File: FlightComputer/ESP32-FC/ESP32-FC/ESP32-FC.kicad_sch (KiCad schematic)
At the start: 0 parts

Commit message: Added USB Connection
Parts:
- added C1: C, symbol Device:C
- added J1: USB_C_Receptacle_USB2.0_16P, symbol Connector:USB_C_Receptacle_USB2.0_16P
- added R1: R, symbol Device:R
- added R2, R3: 5K1, symbol Device:R
- added R4, R5: 27, symbol Device:R
- added U1: ESP32-S3-WROOM-1, RF_Module:ESP32-S3-WROOM-1, symbol RF_Module:ESP32-S3-WROOM-1
- added U2: AP2112K-3.3, Package_TO_SOT_SMD:SOT-23-5, symbol Regulator_Linear:AP2112K-3.3
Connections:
- new net: J1.A5 (CC1), R2.1
- new net: J1.B5 (CC2), R3.1
- new net +5V: J1.A4 (VBUS), J1.A9 (VBUS), J1.B4 (VBUS), J1.B9 (VBUS)
- new net GND: J1.A1 (GND), J1.A12 (GND), J1.B1 (GND), J1.B12 (GND), J1.S1 (SHIELD), R2.2, R3.2, U1.1 (GND), U1.40 (GND), U1.41 (GND)
- new net USB_D+: J1.A6 (D+), J1.B6 (D+), R5.1, R5.2, U1.14 (USB_D+)
- new net USB_D-: J1.A7 (D-), J1.B7 (D-), R4.1, R4.2, U1.13 (USB_D-)
- no-connect marks 0 -> 2

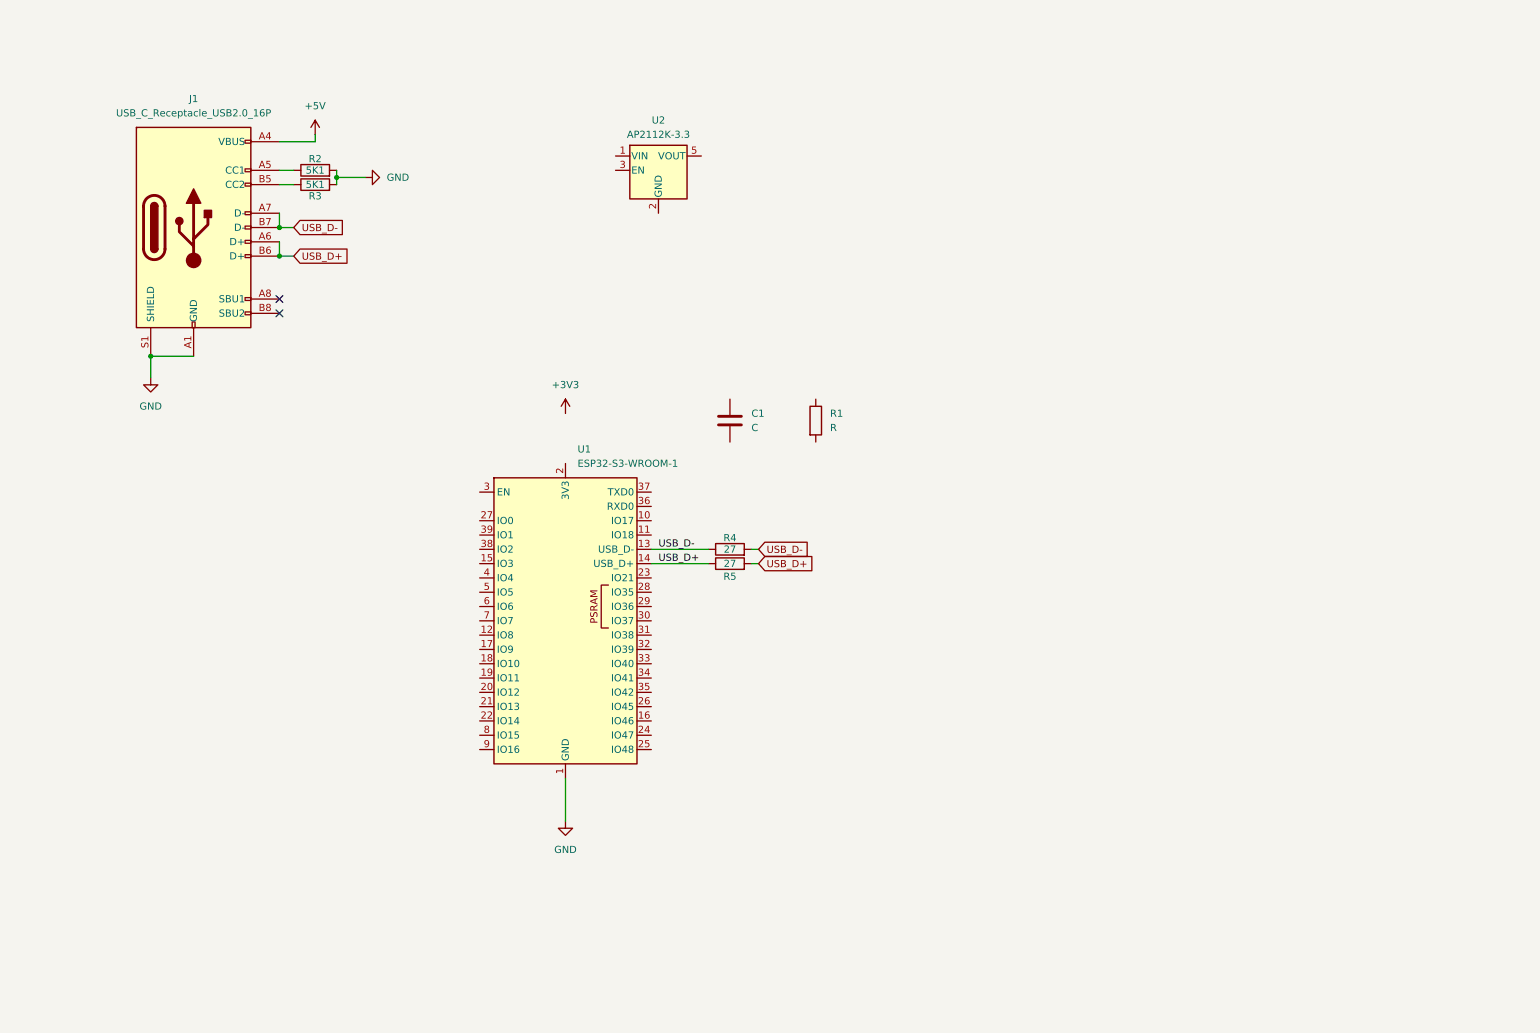
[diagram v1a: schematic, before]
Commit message: Added MPU
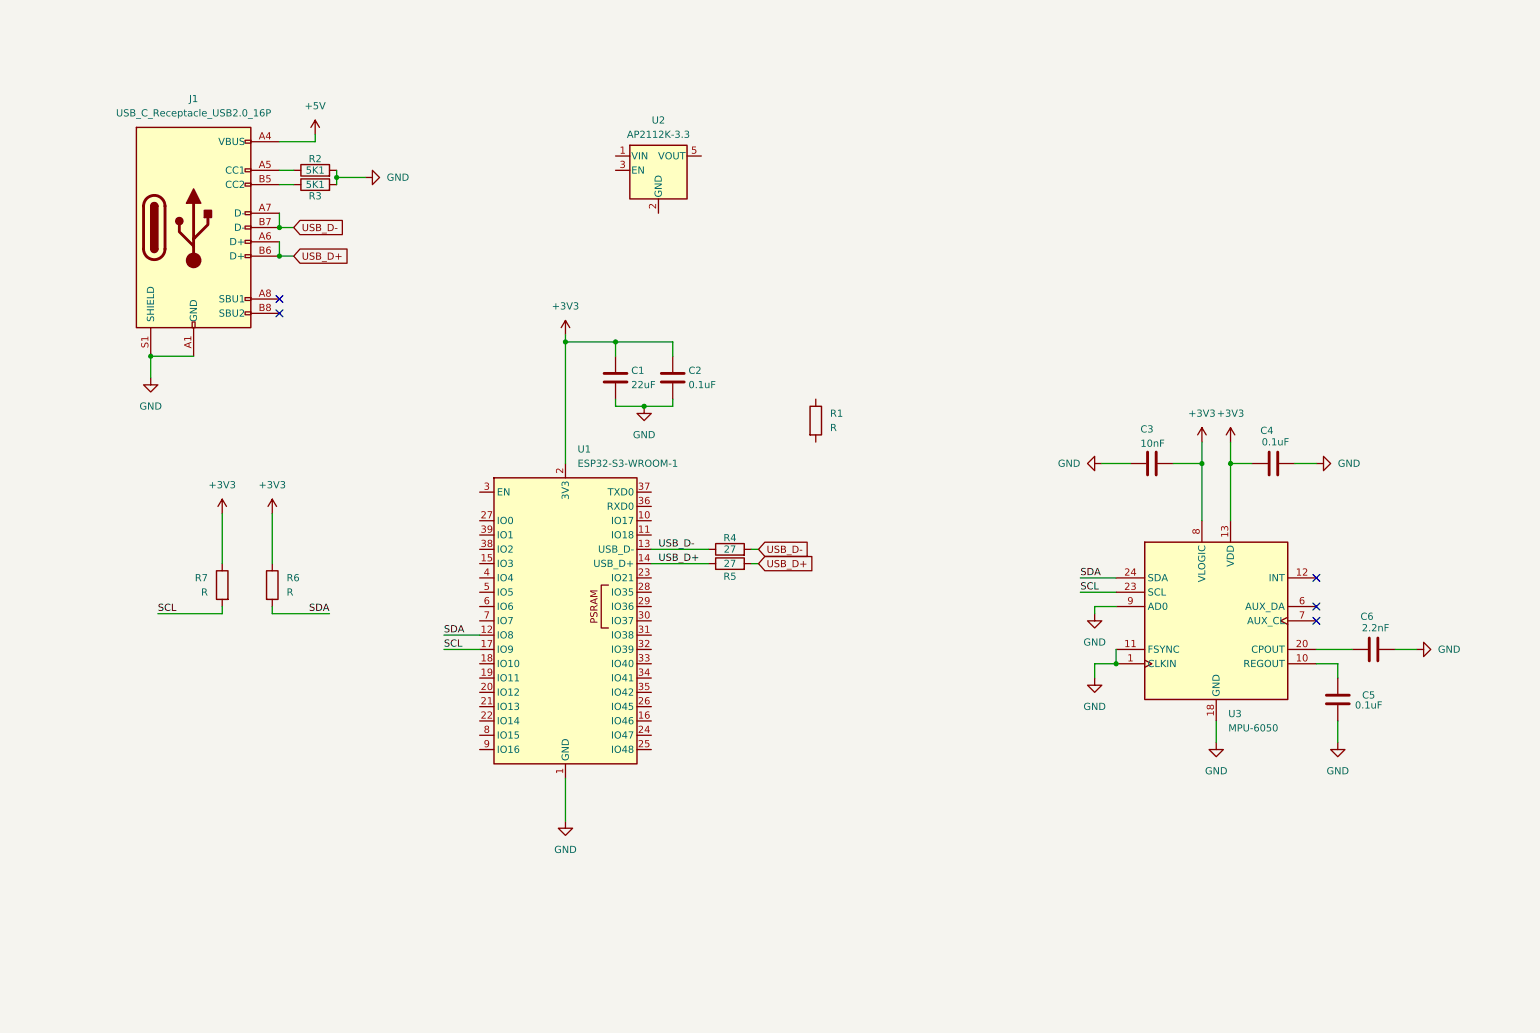
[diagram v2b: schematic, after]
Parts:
- added C2, C4, C5: 0.1uF, symbol Device:C
- added C3: 10nF, symbol Device:C
- added C6: 2.2nF, symbol Device:C
- added R6, R7: R, symbol Device:R
- added U3: MPU-6050, Sensor_Motion:InvenSense_QFN-24_4x4mm_P0.5mm, symbol Sensor_Motion:MPU-6050
- C1: value C -> 22uF
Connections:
- net +3V3: now also C1.1, U1.2 (3V3), C2.1, C3.1, C4.1, R6.1, R7.1, U3.13 (VDD), U3.8 (VLOGIC)
- net GND: now also C1.2, C2.2, C3.2, C4.2, C5.2, C6.2, U3.1 (CLKIN), U3.11 (FSYNC), U3.18 (GND), U3.9 (AD0)
- net SDA: now reaches U1.12 (IO8)
- net SDA: now also R6.2, U3.24 (SDA)
- net SCL: now reaches U1.17 (IO9)
- net SCL: now also R7.2, U3.23 (SCL)
- new net: C6.1, U3.20 (CPOUT)
- new net: C5.1, U3.10 (REGOUT)
- no-connect marks 2 -> 5
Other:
- moved on the sheet: C1

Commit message: Addd ICM
- Removed MPU 6050
- Added ICM-42670-P
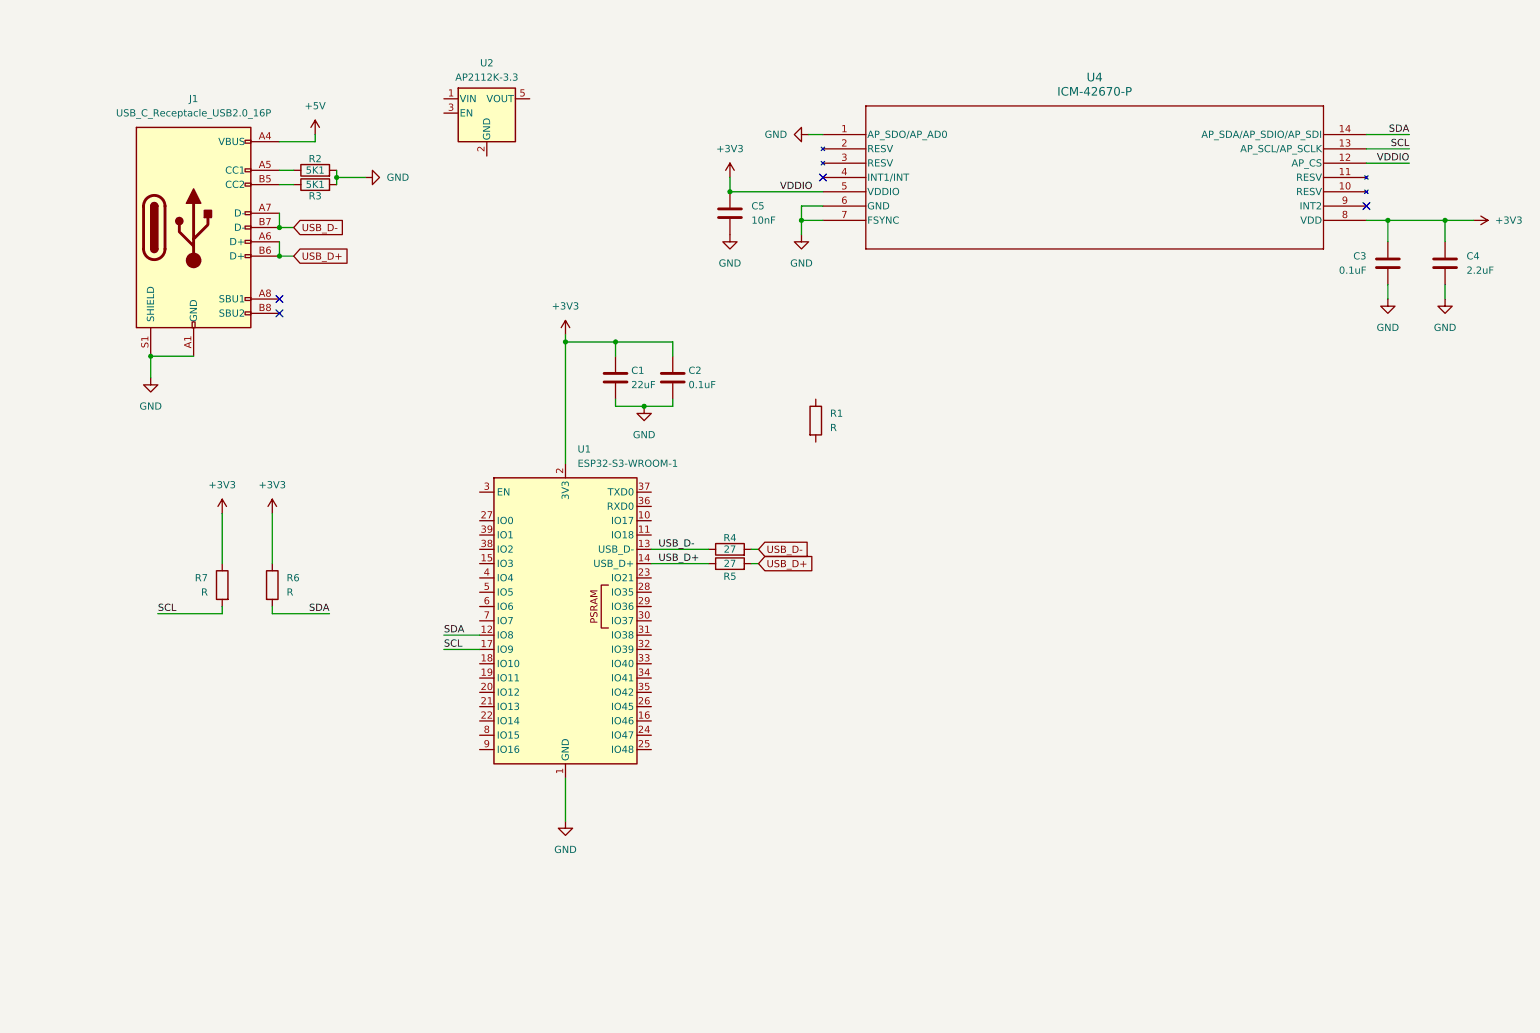
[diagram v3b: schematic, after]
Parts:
- removed C6: 2.2nF, symbol Device:C
- removed U3: MPU-6050, Sensor_Motion:InvenSense_QFN-24_4x4mm_P0.5mm, symbol Sensor_Motion:MPU-6050
- added U4: ICM-42670-P, LGA14_2.5X3X0.76_IVS, symbol ICM-42670-P:ICM-42670-P
- C3: value 10nF -> 0.1uF
- C4: value 0.1uF -> 2.2uF
- C5: value 0.1uF -> 10nF
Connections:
- net +3V3: now also C5.1, U4.12 (AP_CS), U4.5 (VDDIO), U4.8 (VDD)
- net GND: now also U4.1 (AP_SDO/AP_AD0), U4.6 (GND), U4.7 (FSYNC)
- net SCL: now also U4.13 (AP_SCL/AP_SCLK)
- net SDA: now also U4.14 (AP_SDA/AP_SDIO/AP_SDI)
- no-connect marks 5 -> 4
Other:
- moved on the sheet: U2

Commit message: Added ICP
- Added pressure sensor module
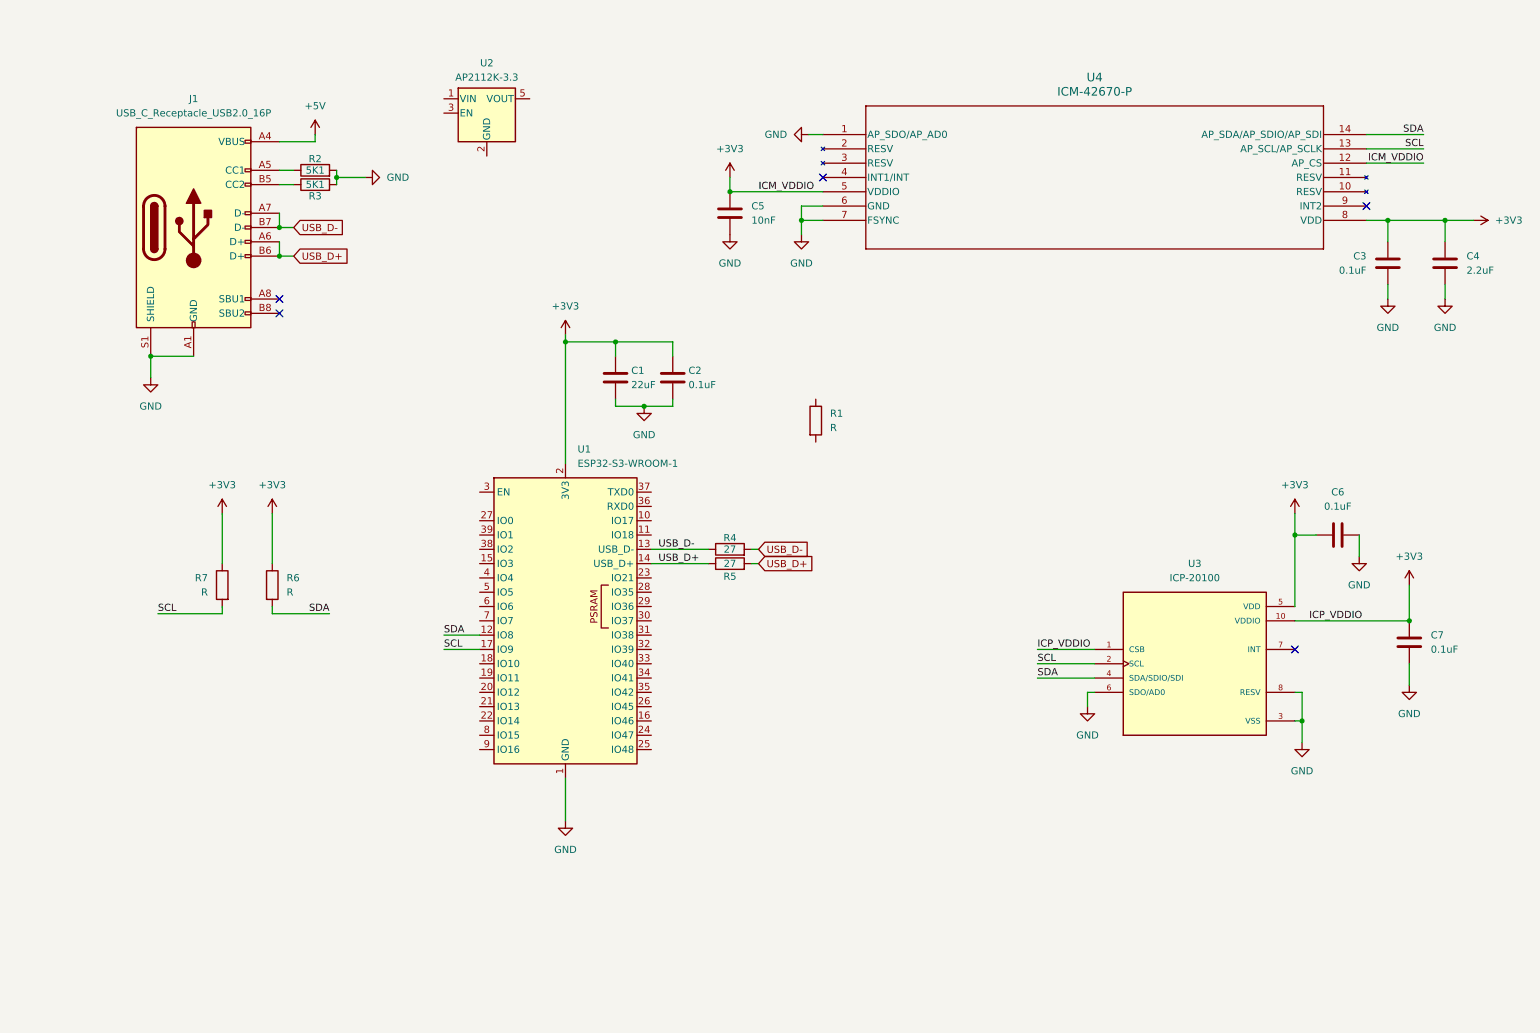
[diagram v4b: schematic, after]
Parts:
- added C6, C7: 0.1uF, symbol Device:C
- added U3: ICP-20100, ICP-20100:PQFN50P200X200X85-10N, symbol ICP-20100:ICP-20100
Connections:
- net +3V3: now also C6.2, C7.1, U3.1 (CSB), U3.10 (VDDIO), U3.5 (VDD)
- net GND: now also C6.1, C7.2, U3.3 (VSS), U3.6 (SDO/AD0), U3.8 (RESV), U3.9 (RESV)
- net SCL: now also U3.2 (SCL)
- net SDA: now also U3.4 (SDA/SDIO/SDI)
- no-connect marks 4 -> 5

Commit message: Layout Creation
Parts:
- C1, C2, C3, C4, C5, C6, C7: footprint (none) -> Capacitor_SMD:C_0805_2012Metric_Pad1.18x1.45mm_HandSolder
- J1: footprint (none) -> Connector_USB:USB_C_Receptacle_Palconn_UTC16-G
- R1, R2, R3, R4, R5, R6, R7: footprint (none) -> Resistor_SMD:R_0805_2012Metric_Pad1.20x1.40mm_HandSolder
- U4: footprint LGA14_2.5X3X0.76_IVS -> ICM-42670-L:LGA14_2.5X3X0.76_IVS-L
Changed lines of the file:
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@@
 	(title_block
 		(title "ESP32 Flight Computer")
-		(date "2026-03-09")
+		(date "2026-03-19")
 		(rev "v1.0")
 		(comment 1 "CANSAT STECI Competition 2026")
@@
 			)
 		)
-		(property "Footprint" ""
+		(property "Footprint" "Capacitor_SMD:C_0805_2012Metric_Pad1.18x1.45mm_HandSolder"
 			(at 134.3152 83.82 0)
 			(effects
@@
 			)
 		)
-		(property "Footprint" ""
+		(property "Footprint" "Capacitor_SMD:C_0805_2012Metric_Pad1.18x1.45mm_HandSolder"
 			(at 259.3848 63.5 0)
 			(effects
@@
 			)
 		)
-		(property "Footprint" ""
+		(property "Footprint" "Capacitor_SMD:C_0805_2012Metric_Pad1.18x1.45mm_HandSolder"
 			(at 265.1252 130.81 0)
 			(effects
@@
 			)
 		)
-		(property "Footprint" ""
+		(property "Footprint" "Capacitor_SMD:C_0805_2012Metric_Pad1.18x1.45mm_HandSolder"
 			(at 144.4752 54.61 0)
 			(effects
@@
 			)
 		)
-		(property "Footprint" ""
+		(property "Footprint" "Resistor_SMD:R_0805_2012Metric_Pad1.20x1.40mm_HandSolder"
 			(at 55.118 116.84 90)
 			(effects
@@
 			)
 		)
-		(property "Footprint" ""
+		(property "Footprint" "Capacitor_SMD:C_0805_2012Metric_Pad1.18x1.45mm_HandSolder"
 			(at 271.4752 63.5 0)
 			(effects
@@
 			)
 		)
-		(property "Footprint" ""
+		(property "Footprint" "Capacitor_SMD:C_0805_2012Metric_Pad1.18x1.45mm_HandSolder"
 			(at 124.1552 83.82 0)
 			(effects
@@
 			)
 		)
-		(property "Footprint" ""
+		(property "Footprint" "Resistor_SMD:R_0805_2012Metric_Pad1.20x1.40mm_HandSolder"
 			(at 156.972 87.63 90)
 			(effects
@@
 			)
 		)
-		(property "Footprint" ""
+		(property "Footprint" "Connector_USB:USB_C_Receptacle_Palconn_UTC16-G"
 			(at 52.07 53.34 0)
 			(effects
@@
 			)
 		)
-		(property "Footprint" ""
+		(property "Footprint" "Resistor_SMD:R_0805_2012Metric_Pad1.20x1.40mm_HandSolder"
 			(at 69.85 47.498 90)
 			(effects
@@
 			)
 		)
-		(property "Footprint" ""
+		(property "Footprint" "Resistor_SMD:R_0805_2012Metric_Pad1.20x1.40mm_HandSolder"
 			(at 60.452 116.84 90)
 			(effects
@@
 			)
 		)
-		(property "Footprint" "LGA14_2.5X3X0.76_IVS"
+		(property "Footprint" "ICM-42670-L:LGA14_2.5X3X0.76_IVS-L"
 			(at 160.02 36.83 0)
 			(effects
@@
 			)
 		)
-		(property "Footprint" ""
+		(property "Footprint" "Resistor_SMD:R_0805_2012Metric_Pad1.20x1.40mm_HandSolder"
 			(at 143.51 114.808 90)
 			(effects
@@
 			)
 		)
-		(property "Footprint" ""
+		(property "Footprint" "Resistor_SMD:R_0805_2012Metric_Pad1.20x1.40mm_HandSolder"
 			(at 143.51 112.268 90)
 			(effects
@@
 			)
 		)
-		(property "Footprint" ""
+		(property "Footprint" "Resistor_SMD:R_0805_2012Metric_Pad1.20x1.40mm_HandSolder"
 			(at 69.85 44.958 90)
 			(effects
@@
 			)
 		)
-		(property "Footprint" ""
+		(property "Footprint" "Capacitor_SMD:C_0805_2012Metric_Pad1.18x1.45mm_HandSolder"
 			(at 247.65 108.9152 0)
 			(effects
